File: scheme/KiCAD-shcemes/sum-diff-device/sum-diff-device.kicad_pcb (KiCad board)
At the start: 2 copper layers, 128 x 157 mm, 75 parts, among them J1 A1, J10 B2, J11 B3, J12 B4, J13 B5, J14 B6, J15 B7, J16 B8, J17 SUM, J18 DIFF, J19 O1, J2 A2, J20 O2, J21 O3, J22 O4, J23 O5, J24 O6, J25 O7, J26 O8, J27 1, J28 1, J3 A3, J4 A4, J5 A5, J6 A6, J7 A7, J8 A8, J9 B1, U1 SN74HC86N, U10 SN74HC08N, U11 SN74HC08N, U12 SN74HC27N, U13 SN74HC27N, U14 SN74HC05N, U15 SN74HC32N, U16 SN74HC08N, U17 SN74HC08N, U2 SN74HC86N, U3 SN74HC86N, U4 SN74HC86N, U5 SN74HC86N, U6 SN74HC86N, U7 SN74HC08N, U8 SN74HC08N, U9 SN74HC08N

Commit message: feat: Complete pcb for SUM/DIFF device.
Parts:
- moved C17 208.7 mm to (144.1, 55.8)
- moved J26 208.3 mm to (104.7, 33.0)
- moved C15 208.3 mm to (104.8, 55.3)
- moved C18 208.3 mm to (41.6, 169.1)
- moved C2 208.3 mm to (64.7, 94.0)
- moved C4 208.3 mm to (104.8, 94.0)
- moved C5 208.3 mm to (124.8, 94.1)
- moved C7 208.3 mm to (45.5, 122.0)
- moved J20 208.3 mm to (89.5, 33.0)
- moved J23 208.3 mm to (97.1, 33.0)
- moved J28 208.3 mm to (45.6, 177.0)
- moved R11 208.3 mm to (94.4, 69.8)
- moved R5 208.3 mm to (133.7, 133.1)
- moved R6 208.3 mm to (133.7, 128.5)
- moved U1 208.3 mm to (47.1, 105.7)
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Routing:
- net GND: track 1458.0 -> 1371.8 mm, vias 8 -> 14
- net +5V: track 1109.0 -> 1187.9 mm, vias 6 -> 11
- net Net-(U14-Pad6): track 46.9 -> 92.7 mm
- net Net-(U12-Pad9): track 0.00 -> 43.6 mm
- net Net-(U10-Pad11): track 0.00 -> 43.5 mm
- net Net-(U14-Pad4): track 51.5 -> 89.9 mm
- net Net-(U12-Pad11): track 0.00 -> 37.9 mm
- net Net-(U12-Pad10): track 0.00 -> 37.7 mm, vias 0 -> 2
- net Net-(U13-Pad12): track 0.00 -> 37.0 mm
- net Net-(U10-Pad3): track 0.00 -> 32.3 mm
- net Net-(U12-Pad5): track 0.00 -> 30.5 mm
- net Net-(U9-Pad11): track 0.00 -> 30.3 mm
- net Net-(U10-Pad8): track 0.00 -> 26.2 mm
- net Net-(U13-Pad8): track 0.00 -> 25.6 mm
- net Net-(U12-Pad6): track 0.00 -> 24.5 mm
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
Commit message: feat: last version of pcb
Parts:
- R1, R10, R11, R12, R2, R3, R4, R5, R6, R7, R8, R9: footprint Resistor_THT:R_Axial_DIN0411_L9.9mm_D3.6mm_P5.08mm_Vertical -> Resistor_THT:R_Axial_DIN0204_L3.6mm_D1.6mm_P5.08mm_Vertical
- moved C16 0.32 mm to (64.8, 55.0)
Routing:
- net +5V: track 1187.9 -> 1151.6 mm
- net Net-(U17-Pad4): track 74.1 -> 64.6 mm, vias 1 -> 2
- net Net-(U15-Pad3): track 180.8 -> 172.1 mm
- net GND: track 1371.8 -> 1363.3 mm
- net Net-(J22-Pad1): track 46.0 -> 47.8 mm
- net Net-(J23-Pad1): track 65.0 -> 66.3 mm
- net Net-(U17-Pad12): track 53.6 -> 54.7 mm
- net Net-(J21-Pad1): track 57.2 -> 58.1 mm
- net Net-(U1-Pad3): track 52.3 -> 53.2 mm
- net Net-(U1-Pad11): track 43.4 -> 44.1 mm

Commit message: feat: Changed pcb for sum-diff device
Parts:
- removed J10: B2, Connector_Pin:Pin_D0.7mm_L6.5mm_W1.8mm_FlatFork
- removed J11: B3, Connector_Pin:Pin_D0.7mm_L6.5mm_W1.8mm_FlatFork
- removed J12: B4, Connector_Pin:Pin_D0.7mm_L6.5mm_W1.8mm_FlatFork
- removed J13: B5, Connector_Pin:Pin_D0.7mm_L6.5mm_W1.8mm_FlatFork
- removed J14: B6, Connector_Pin:Pin_D0.7mm_L6.5mm_W1.8mm_FlatFork
- removed J15: B7, Connector_Pin:Pin_D0.7mm_L6.5mm_W1.8mm_FlatFork
- removed J16: B8, Connector_Pin:Pin_D0.7mm_L6.5mm_W1.8mm_FlatFork
- removed J17: SUM, Connector_Pin:Pin_D0.7mm_L6.5mm_W1.8mm_FlatFork
- removed J18: DIFF, Connector_Pin:Pin_D0.7mm_L6.5mm_W1.8mm_FlatFork
- removed J19: O1, Connector_Pin:Pin_D0.7mm_L6.5mm_W1.8mm_FlatFork
- removed J20: O2, Connector_Pin:Pin_D0.7mm_L6.5mm_W1.8mm_FlatFork
- removed J21: O3, Connector_Pin:Pin_D0.7mm_L6.5mm_W1.8mm_FlatFork
- removed J22: O4, Connector_Pin:Pin_D0.7mm_L6.5mm_W1.8mm_FlatFork
- removed J23: O5, Connector_Pin:Pin_D0.7mm_L6.5mm_W1.8mm_FlatFork
- removed J24: O6, Connector_Pin:Pin_D0.7mm_L6.5mm_W1.8mm_FlatFork
- removed J25: O7, Connector_Pin:Pin_D0.7mm_L6.5mm_W1.8mm_FlatFork
- removed J26: O8, Connector_Pin:Pin_D0.7mm_L6.5mm_W1.8mm_FlatFork
- removed J27, J28: 1, Connector_Pin:Pin_D0.7mm_L6.5mm_W1.8mm_FlatFork
- removed J6: A6, Connector_Pin:Pin_D0.7mm_L6.5mm_W1.8mm_FlatFork
- removed J7: A7, Connector_Pin:Pin_D0.7mm_L6.5mm_W1.8mm_FlatFork
- removed J8: A8, Connector_Pin:Pin_D0.7mm_L6.5mm_W1.8mm_FlatFork
- removed J9: B1, Connector_Pin:Pin_D0.7mm_L6.5mm_W1.8mm_FlatFork
- J1: value A1 -> Conn_01x08_Female; footprint Connector_Pin:Pin_D0.7mm_L6.5mm_W1.8mm_FlatFork -> Connector_PinHeader_2.54mm:PinHeader_1x08_P2.54mm_Vertical
- J2: value A2 -> Conn_01x08_Female; footprint Connector_Pin:Pin_D0.7mm_L6.5mm_W1.8mm_FlatFork -> Connector_PinHeader_2.54mm:PinHeader_1x08_P2.54mm_Vertical
- J3: value A3 -> SUM_DIFF; footprint Connector_Pin:Pin_D0.7mm_L6.5mm_W1.8mm_FlatFork -> Connector_PinSocket_2.54mm:PinSocket_1x02_P2.54mm_Vertical
- J4: value A4 -> Conn_01x08_Male; footprint Connector_Pin:Pin_D0.7mm_L6.5mm_W1.8mm_FlatFork -> Connector_PinHeader_2.54mm:PinHeader_1x08_P2.54mm_Vertical
- J5: value A5 -> Conn_01x02_Male; footprint Connector_Pin:Pin_D0.7mm_L6.5mm_W1.8mm_FlatFork -> Connector_PinSocket_2.54mm:PinSocket_1x02_P2.54mm_Vertical
- moved J3 282.4 mm to (288.3, 270.7), turned to 90 degrees
- moved R12 274.5 mm to (276.2, 270.6)
- moved R11 264.8 mm to (276.1, 262.5), turned to -90 degrees
- moved R9 262.0 mm to (296.8, 262.6), turned to 90 degrees
- moved R10 256.7 mm to (293.9, 262.5), turned to 90 degrees
- moved U15 256.4 mm to (283.9, 251.9)
- moved C15 255.8 mm to (281.4, 240.4)
- moved R7 253.4 mm to (296.4, 241.8), turned to -90 degrees
- moved R8 248.2 mm to (293.6, 241.8), turned to -90 degrees
- moved C16 236.6 mm to (248.8, 203.8), turned to 90 degrees
- moved U16 236.2 mm to (260.7, 201.2), turned to 90 degrees
- moved J1 224.2 mm to (241.7, 202.1)
- moved J4 220.8 mm to (281.8, 190.9)
- moved J2 208.5 mm to (241.3, 193.0)
- moved U1 202.0 mm to (208.7, 226.9)
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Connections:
- J5 pad 1: Net-(J5-Pad1) -> +5V
- U1 pad 1: Net-(J1-Pad1) -> Net-(J1-Pad8)
- U1 pad 10: Net-(J10-Pad1) -> Net-(J2-Pad7)
- U1 pad 2: Net-(J9-Pad1) -> Net-(J2-Pad8)
- U1 pad 4: Net-(J9-Pad1) -> Net-(J2-Pad8)
- U1 pad 5: Net-(J18-Pad1) -> Net-(J3-Pad1)
- U1 pad 9: Net-(J2-Pad1) -> Net-(J1-Pad7)
- U10 pad 1: Net-(J5-Pad1) -> Net-(J1-Pad4)
- U10 pad 12: Net-(J6-Pad1) -> Net-(U10-Pad12)
- U10 pad 4: Net-(J6-Pad1) -> Net-(U10-Pad12)
- U11 pad 1: Net-(J7-Pad1) -> Net-(J1-Pad2)
- U11 pad 2: Net-(J15-Pad1) -> Net-(J2-Pad2)
- U11 pad 5: Net-(J15-Pad1) -> Net-(J2-Pad2)
- U11 pad 9: Net-(J7-Pad1) -> Net-(J1-Pad2)
- U14 pad 10: Net-(J15-Pad1) -> Net-(J2-Pad2)
- U15 pad 1: Net-(J17-Pad1) -> Net-(J3-Pad2)
- U15 pad 2: Net-(J18-Pad1) -> Net-(J3-Pad1)
- U16 pad 11: Net-(J22-Pad1) -> Net-(J4-Pad5)
- U16 pad 3: Net-(J19-Pad1) -> Net-(J4-Pad8)
- U16 pad 6: Net-(J20-Pad1) -> Net-(U16-Pad6)
- U16 pad 8: Net-(J21-Pad1) -> Net-(J4-Pad6)
- U17 pad 11: Net-(J26-Pad1) -> Net-(J4-Pad1)
- U17 pad 3: Net-(J23-Pad1) -> Net-(J4-Pad4)
- U17 pad 6: Net-(J24-Pad1) -> Net-(U17-Pad6)
- U17 pad 8: Net-(J25-Pad1) -> Net-(J4-Pad2)
- U2 pad 1: Net-(J10-Pad1) -> Net-(J2-Pad7)
- U2 pad 12: Net-(J11-Pad1) -> Net-(U2-Pad12)
- U2 pad 13: Net-(J18-Pad1) -> Net-(J3-Pad1)
- U2 pad 2: Net-(J18-Pad1) -> Net-(J3-Pad1)
- U2 pad 4: Net-(J3-Pad1) -> Net-(J1-Pad6)
- U2 pad 5: Net-(J11-Pad1) -> Net-(U2-Pad12)
- U3 pad 10: Net-(J18-Pad1) -> Net-(J3-Pad1)
- U3 pad 12: Net-(J5-Pad1) -> Net-(J1-Pad4)
- U3 pad 13: Net-(J13-Pad1) -> Net-(J2-Pad4)
- U3 pad 4: Net-(J4-Pad1) -> Net-(J1-Pad5)
- U3 pad 5: Net-(J12-Pad1) -> Net-(J2-Pad5)
- U3 pad 9: Net-(J12-Pad1) -> Net-(J2-Pad5)
- U4 pad 10: Net-(J14-Pad1) -> Net-(J2-Pad3)
- U4 pad 4: Net-(J13-Pad1) -> Net-(J2-Pad4)
- U4 pad 5: Net-(J18-Pad1) -> Net-(J3-Pad1)
- U4 pad 9: Net-(J6-Pad1) -> Net-(U10-Pad12)
- U5 pad 1: Net-(J14-Pad1) -> Net-(J2-Pad3)
- U5 pad 12: Net-(J15-Pad1) -> Net-(J2-Pad2)
- U5 pad 13: Net-(J18-Pad1) -> Net-(J3-Pad1)
- U5 pad 2: Net-(J18-Pad1) -> Net-(J3-Pad1)
- U5 pad 4: Net-(J7-Pad1) -> Net-(J1-Pad2)
- U5 pad 5: Net-(J15-Pad1) -> Net-(J2-Pad2)
- U5 pad 9: Net-(J15-Pad1) -> Net-(J2-Pad2)
- U6 pad 1: Net-(J16-Pad1) -> Net-(J2-Pad1)
- U6 pad 2: Net-(J8-Pad1) -> Net-(J1-Pad1)
- U7 pad 1: Net-(J1-Pad1) -> Net-(J1-Pad8)
- U7 pad 12: Net-(J2-Pad1) -> Net-(J1-Pad7)
- U7 pad 4: Net-(J2-Pad1) -> Net-(J1-Pad7)
- U8 pad 1: Net-(J3-Pad1) -> Net-(J1-Pad6)
- U8 pad 12: Net-(J4-Pad1) -> Net-(J1-Pad5)
- U8 pad 9: Net-(J3-Pad1) -> Net-(J1-Pad6)
- U9 pad 4: Net-(J4-Pad1) -> Net-(J1-Pad5)
- U9 pad 9: Net-(J5-Pad1) -> Net-(J1-Pad4)
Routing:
- net GND: track 1363.3 -> 630.4 mm, vias 14 -> 4
- net +5V: track 1151.6 -> 488.0 mm, vias 11 -> 0
- net Net-(J18-Pad1): track 282.1 -> 0.00 mm, vias 2 -> 0
- net Net-(J2-Pad2): track 0.00 -> 173.0 mm, vias 0 -> 2
- net Net-(J15-Pad1): track 172.8 -> 0.00 mm
- net Net-(J1-Pad2): track 0.00 -> 99.4 mm
- net Net-(J5-Pad1): track 83.0 -> 0.00 mm
- net Net-(U10-Pad12): track 0.00 -> 78.2 mm
- net Net-(J25-Pad1): track 77.8 -> 0.00 mm
- net Net-(J24-Pad1): track 77.3 -> 0.00 mm
- net Net-(J4-Pad1): track 83.2 -> 7.74 mm, vias 2 -> 0
- net Net-(J2-Pad5): track 0.00 -> 74.4 mm, vias 0 -> 1
- net Net-(J1-Pad5): track 0.00 -> 73.7 mm
- net Net-(J26-Pad1): track 73.1 -> 0.00 mm
- net Net-(J1-Pad6): track 0.00 -> 72.9 mm
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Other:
- board size 128 x 157 mm -> 100 x 100 mm

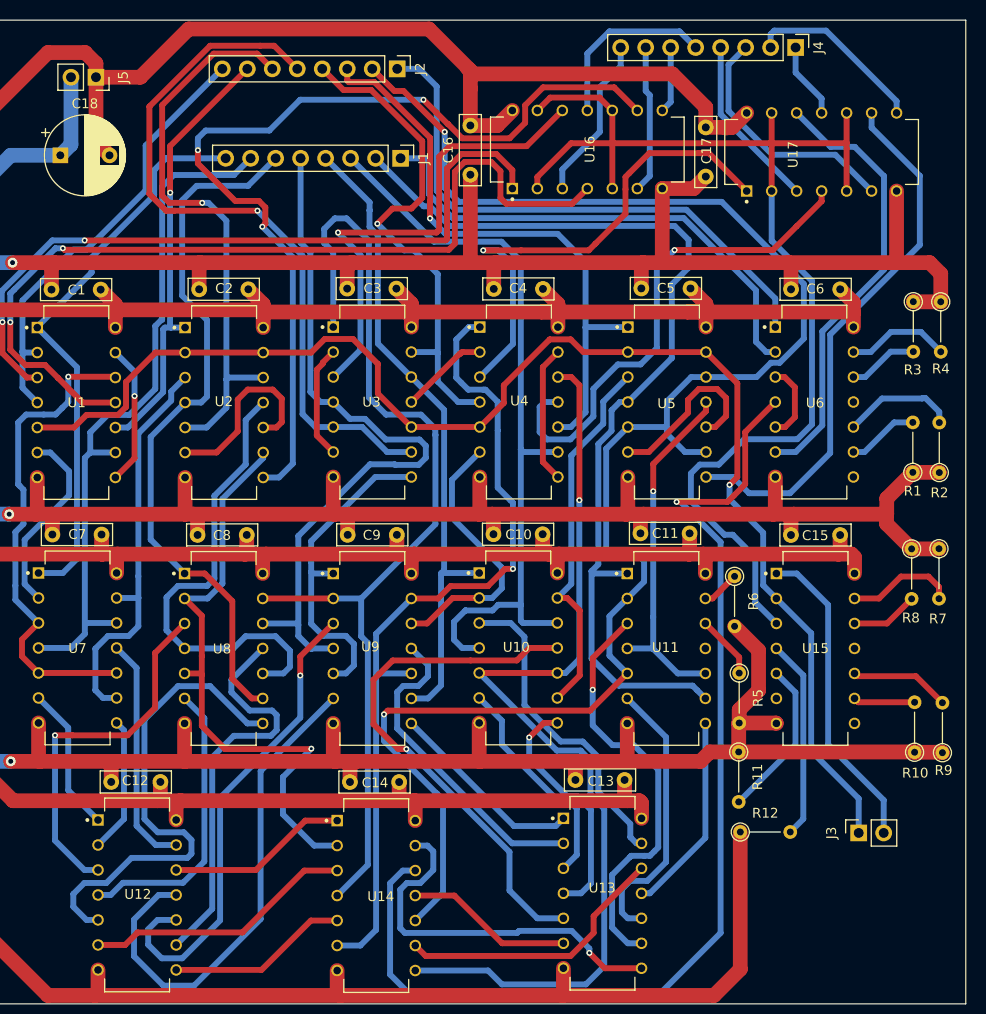
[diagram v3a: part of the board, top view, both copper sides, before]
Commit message: feat: Created build for jlcpcb.
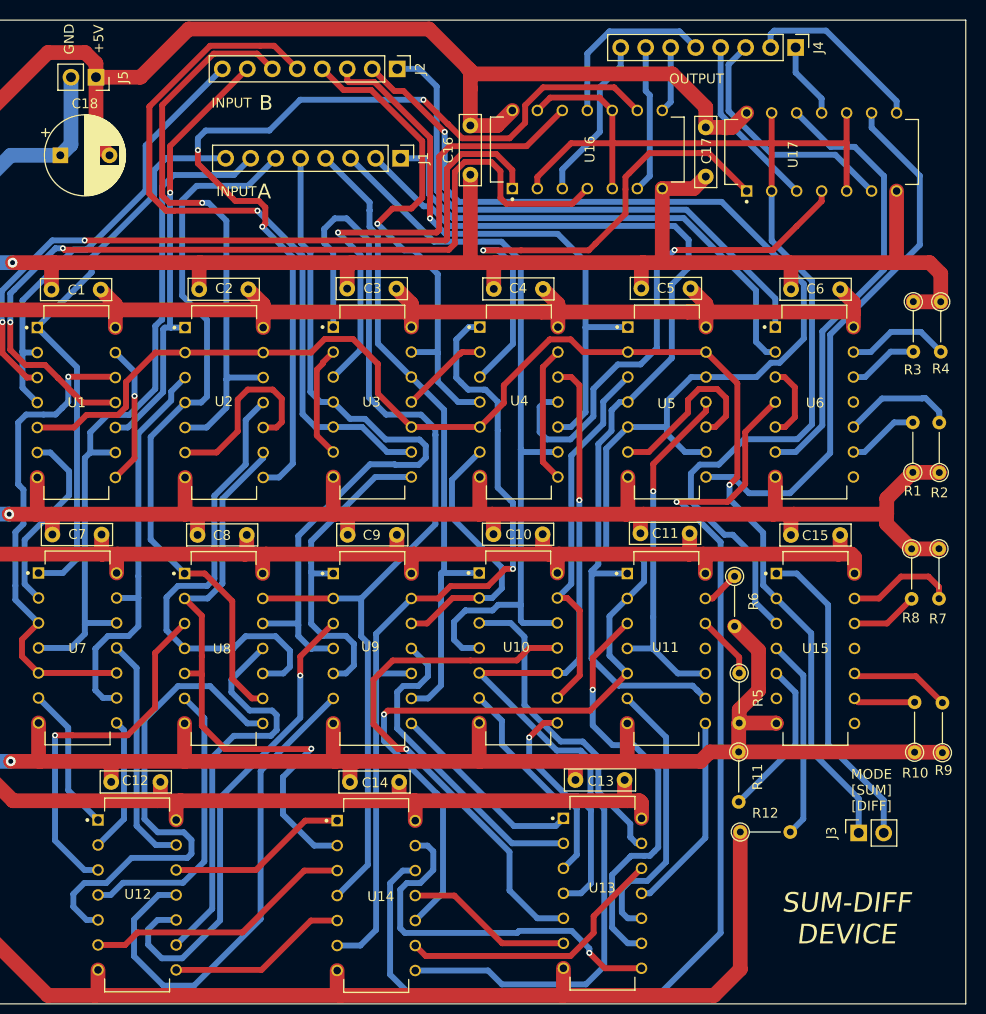
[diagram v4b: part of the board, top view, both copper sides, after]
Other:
- board text added: "+5V"
- board text added: "A"
- board text added: "B"
- board text added: "GND"
- board text added: "INPUT"
- board text added: "MODE [SUM] [DIFF]"
- board text added: "OUTPUT"
- board text added: "SUM-DIFF DEVICE"
